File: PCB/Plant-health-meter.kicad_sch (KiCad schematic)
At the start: 0 parts

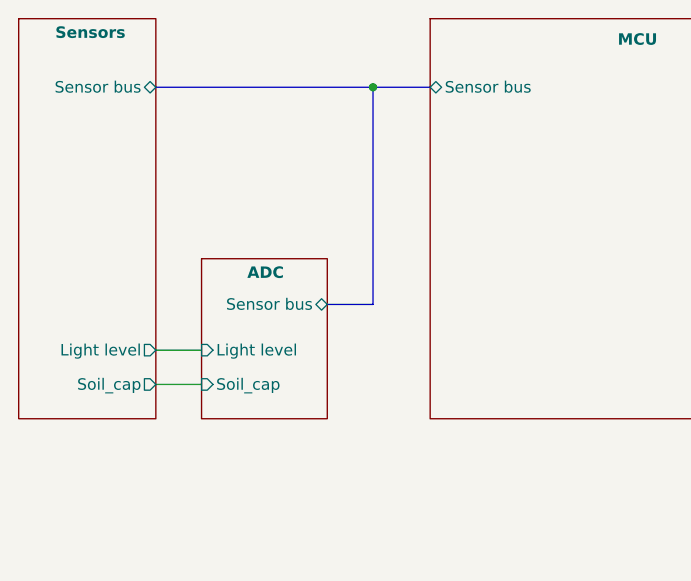
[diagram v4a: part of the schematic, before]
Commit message: removed usb port library
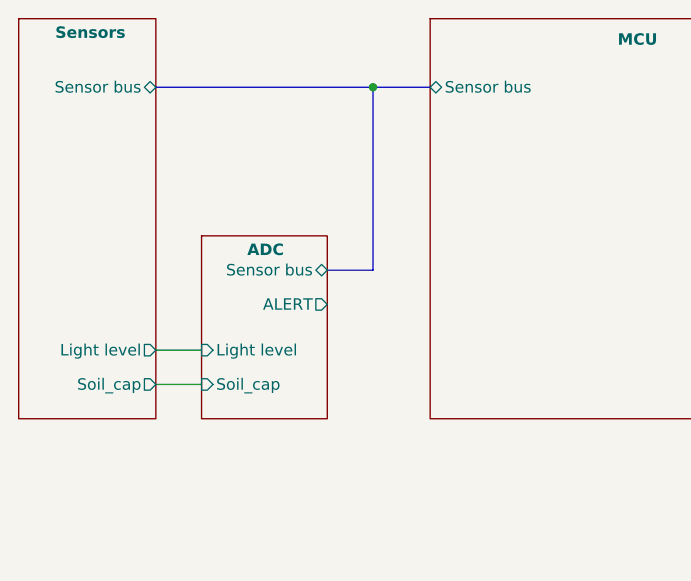
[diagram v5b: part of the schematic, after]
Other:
- sheet ADC ports: added ALERT; removed none
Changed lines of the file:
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@@
 	(bus
 		(pts
-			(xy 127 109.22) (xy 132.08 109.22)
+			(xy 127 105.41) (xy 132.08 105.41)
 		)
 		(stroke
@@
 	(bus
 		(pts
-			(xy 132.08 109.22) (xy 132.08 85.09)
+			(xy 132.08 105.41) (xy 132.08 85.09)
 		)
 		(stroke
@@
 	)
 	(sheet
-		(at 113.03 104.14)
-		(size 13.97 17.78)
+		(at 113.03 101.6)
+		(size 13.97 20.32)
 		(stroke
 			(width 0.1524)
@@
 		)
 		(property "Sheetname" "ADC"
-			(at 118.11 106.426 0)
+			(at 118.11 103.886 0)
 			(effects
 				(font
@@
 		)
 		(property "Sheetfile" "adc.kicad_sch"
-			(at 113.03 123.7746 0)
+			(at 113.03 121.2346 0)
 			(effects
 				(font
@@
 		)
 		(pin "Sensor bus" bidirectional
-			(at 127 109.22 0)
+			(at 127 105.41 0)
 			(effects
 				(font
@@
 			)
 		)
+		(pin "ALERT" output
+			(at 127 109.22 0)
+			(effects
+				(font
+					(size 1.27 1.27)
+				)
+				(justify right)
+			)
+		)

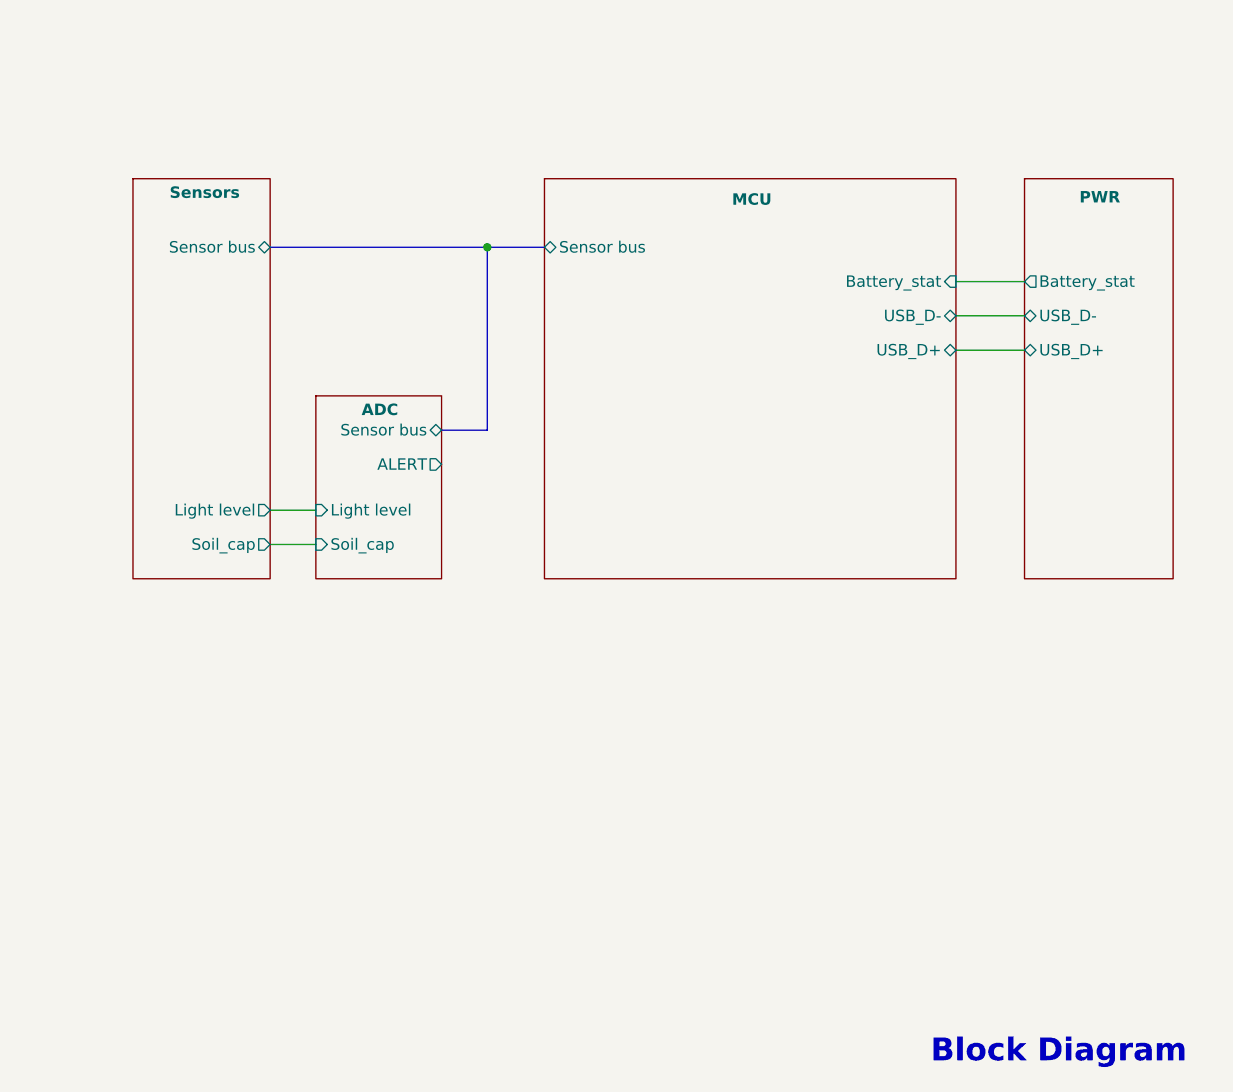
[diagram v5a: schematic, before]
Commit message: Optimized PCB lauout and added Header for LED indicator bar
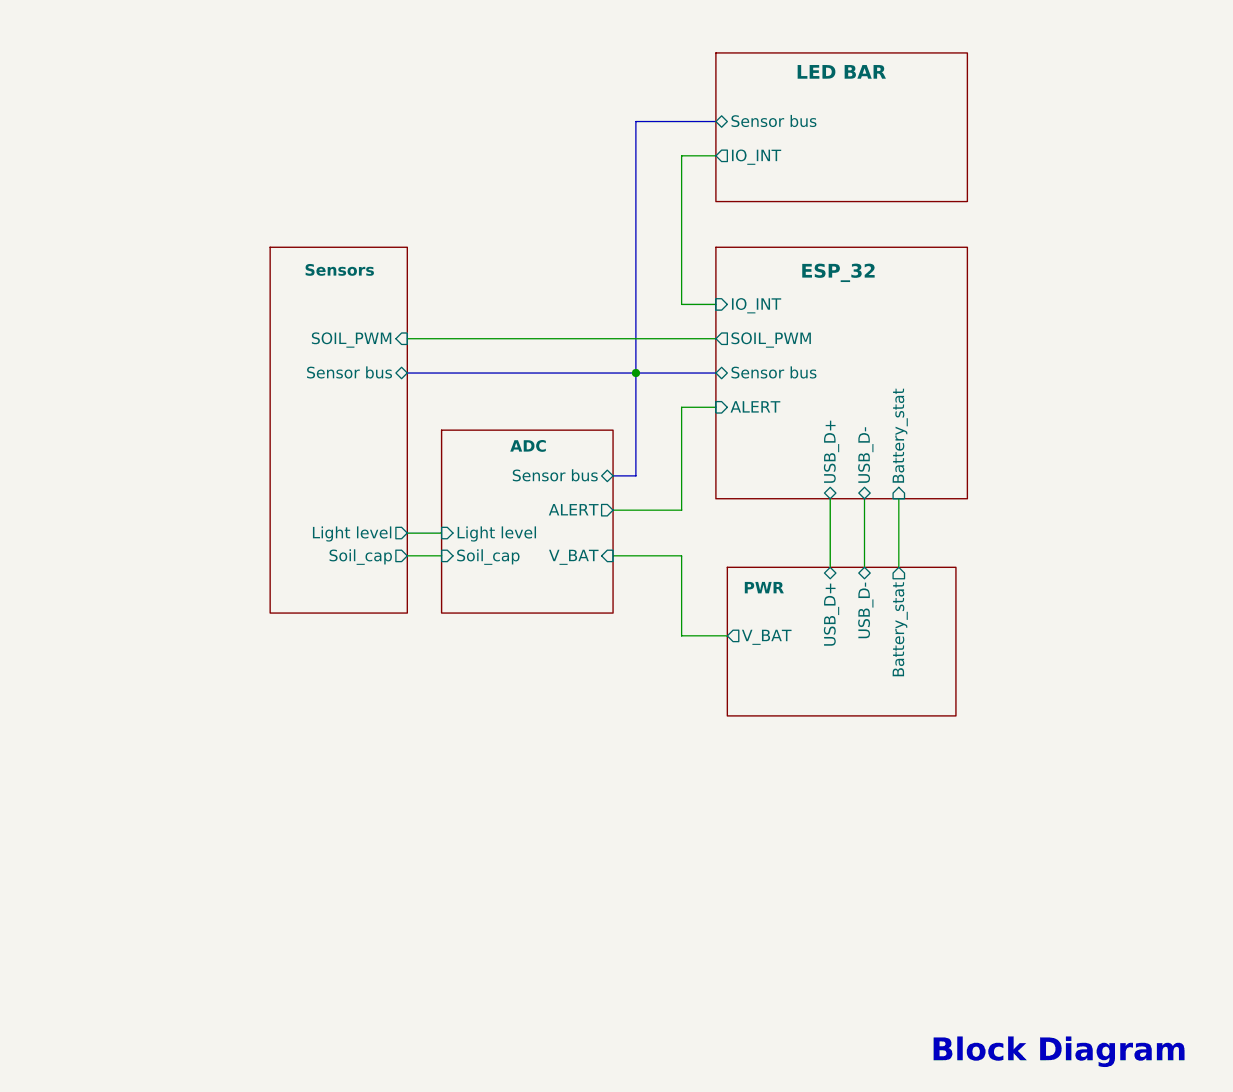
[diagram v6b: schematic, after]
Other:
- sheet MCU renamed ESP_32
- added sheet LED BAR (LEDS.kicad_sch)
- sheet ADC ports: added V_BAT; removed none
- sheet ESP_32 ports: added ALERT, IO_INT, SOIL_PWM; removed none
- sheet PWR ports: added V_BAT; removed none
- sheet Sensors ports: added SOIL_PWM; removed none

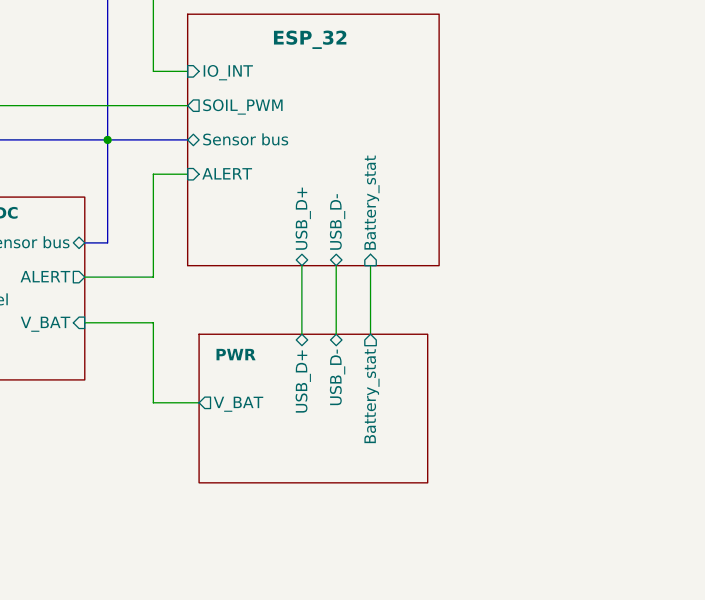
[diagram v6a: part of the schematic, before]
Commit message: ESD protection and Boost UVLO
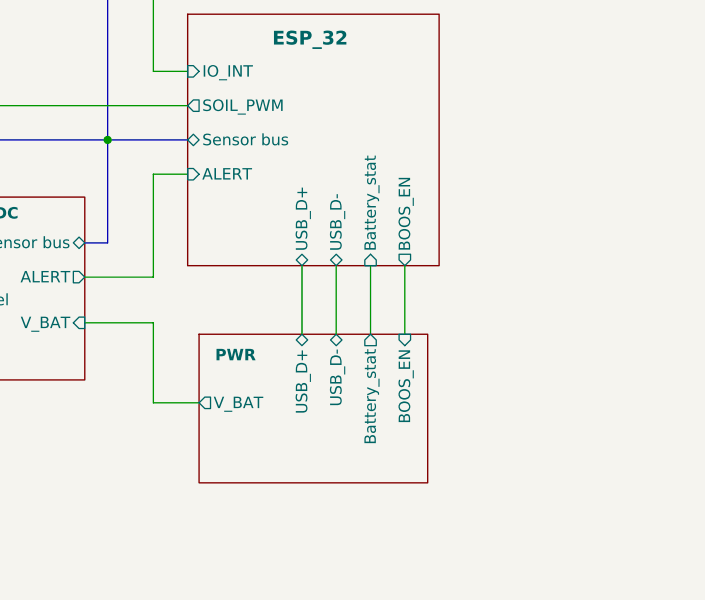
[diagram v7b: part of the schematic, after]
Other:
- sheet ESP_32 ports: added BOOS_EN; removed none
- sheet PWR ports: added BOOS_EN; removed none
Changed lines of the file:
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@@
+	(wire
+		(pts
+			(xy 181.61 113.03) (xy 181.61 120.65)
+		)
+		(stroke
+			(width 0)
+			(type default)
+		)
+	)
 	(wire
 		(pts
@@
 			)
 		)
+		(pin "BOOS_EN" input
+			(at 181.61 120.65 90)
+			(effects
+				(font
+					(size 1.27 1.27)
+				)
+				(justify right)
+			)
+		)
 		(instances
 			(project "Plant-health-meter"
@@
 			(effects
 				(font
+					(size 1.27 1.27)
+				)
+				(justify left)
+			)
+		)
+		(pin "BOOS_EN" output
+			(at 181.61 113.03 270)
+			(effects
+				(font
